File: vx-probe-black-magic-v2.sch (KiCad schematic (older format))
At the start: 14 parts, among them P1 USB MINI B, U1 stm32f070-qfp48, Y1 8 MHz

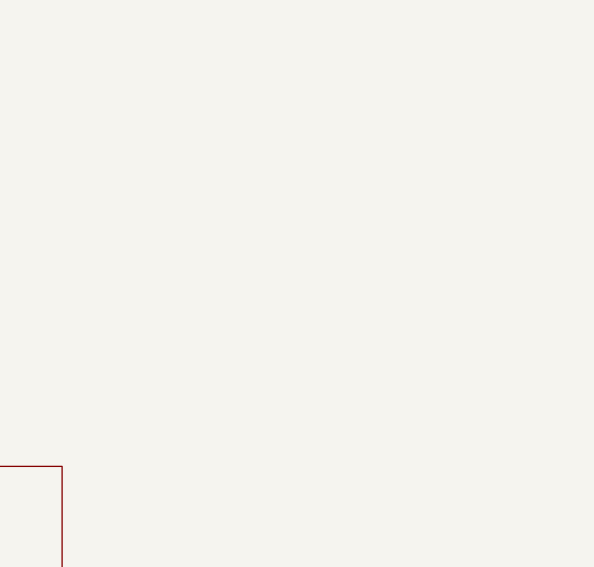
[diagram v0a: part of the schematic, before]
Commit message: added the at45db32 library part
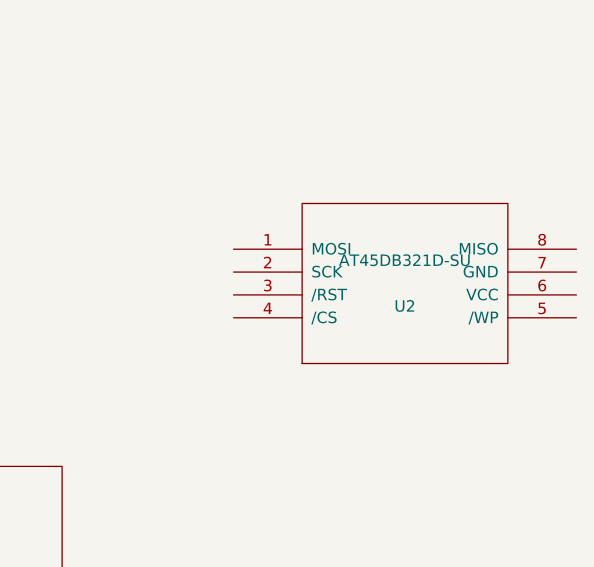
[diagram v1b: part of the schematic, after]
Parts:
- added U2: AT45DB321D-SU, MODULE, symbol AT45DB321D-SU
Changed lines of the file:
@@
 LIBS:valves
 LIBS:stm32f103-qfp48
+LIBS:AT45DB321D-SU
 LIBS:vx-probe-black-magic-v2-cache
 EELAYER 25 0
@@
 $EndComp
 $Comp
-L GND #PWR01
+L GND #PWR4
 U 1 1 57D81245
 P 2200 4200
-F 0 "#PWR01" H 2200 3950 50  0001 C CNN
+F 0 "#PWR4" H 2200 3950 50  0001 C CNN
 F 1 "GND" H 2200 4050 50  0000 C CNN
 F 2 "" H 2200 4200 50  0000 C CNN
@@
 $EndComp
 $Comp
-L +3V3 #PWR02
+L +3V3 #PWR5
 U 1 1 57D815C1
 P 2500 4500
-F 0 "#PWR02" H 2500 4350 50  0001 C CNN
+F 0 "#PWR5" H 2500 4350 50  0001 C CNN
 F 1 "+3V3" H 2500 4640 50  0000 C CNN
 F 2 "" H 2500 4500 50  0000 C CNN
@@
 $EndComp
 $Comp
-L GND #PWR03
+L GND #PWR6
 U 1 1 57D81629
 P 2500 5250
-F 0 "#PWR03" H 2500 5000 50  0001 C CNN
+F 0 "#PWR6" H 2500 5000 50  0001 C CNN
 F 1 "GND" H 2500 5100 50  0000 C CNN
 F 2 "" H 2500 5250 50  0000 C CNN
@@
 Connection ~ 1550 6900
 $Comp
-L +3V3 #PWR04
+L +3V3 #PWR1
 U 1 1 57D827E5
 P 1550 6850
-F 0 "#PWR04" H 1550 6700 50  0001 C CNN
+F 0 "#PWR1" H 1550 6700 50  0001 C CNN
 F 1 "+3V3" H 1550 6990 50  0000 C CNN
 F 2 "" H 1550 6850 50  0000 C CNN
@@
 Connection ~ 1550 7200
 $Comp
-L GND #PWR05
+L GND #PWR2
 U 1 1 57D82853
 P 1550 7250
-F 0 "#PWR05" H 1550 7000 50  0001 C CNN
+F 0 "#PWR2" H 1550 7000 50  0001 C CNN
 F 1 "GND" H 1550 7100 50  0000 C CNN
 F 2 "" H 1550 7250 50  0000 C CNN
@@
 	1950 1550 1950 1600
 $Comp
-L GND #PWR06
+L GND #PWR3
 U 1 1 57D8325D
 P 1950 1600
-F 0 "#PWR06" H 1950 1350 50  0001 C CNN
+F 0 "#PWR3" H 1950 1350 50  0001 C CNN
 F 1 "GND" H 1950 1450 50  0000 C CNN
 F 2 "" H 1950 1600 50  0000 C CNN
@@
 Wire Notes Line
 	750  2150 750  600
+$Comp
+L AT45DB321D-SU U2
+U 1 1 57D84EBF
+P 8500 1850
+F 0 "U2" H 8500 1750 50  0000 C CNN
+F 1 "AT45DB321D-SU" H 8500 1950 50  0000 C CNN
+F 2 "MODULE" H 8500 1850 50  0001 C CNN
+F 3 "DOCUMENTATION" H 8500 1850 50  0001 C CNN
+	1    8500 1850
+	1    0    0    -1
+$EndComp
 $EndSCHEMATC

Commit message: assigned the at45db32 part footprint
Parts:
- U2: footprint MODULE -> Housings_SOIC:SOIJ-8_5.3x5.3mm_Pitch1.27mm
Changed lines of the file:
@@
 $EndComp
 $Comp
-L GND #PWR4
+L GND #PWR01
 U 1 1 57D81245
 P 2200 4200
-F 0 "#PWR4" H 2200 3950 50  0001 C CNN
+F 0 "#PWR01" H 2200 3950 50  0001 C CNN
 F 1 "GND" H 2200 4050 50  0000 C CNN
 F 2 "" H 2200 4200 50  0000 C CNN
@@
 $EndComp
 $Comp
-L +3V3 #PWR5
+L +3V3 #PWR02
 U 1 1 57D815C1
 P 2500 4500
-F 0 "#PWR5" H 2500 4350 50  0001 C CNN
+F 0 "#PWR02" H 2500 4350 50  0001 C CNN
 F 1 "+3V3" H 2500 4640 50  0000 C CNN
 F 2 "" H 2500 4500 50  0000 C CNN
@@
 $EndComp
 $Comp
-L GND #PWR6
+L GND #PWR03
 U 1 1 57D81629
 P 2500 5250
-F 0 "#PWR6" H 2500 5000 50  0001 C CNN
+F 0 "#PWR03" H 2500 5000 50  0001 C CNN
 F 1 "GND" H 2500 5100 50  0000 C CNN
 F 2 "" H 2500 5250 50  0000 C CNN
@@
 Connection ~ 1550 6900
 $Comp
-L +3V3 #PWR1
+L +3V3 #PWR04
 U 1 1 57D827E5
 P 1550 6850
-F 0 "#PWR1" H 1550 6700 50  0001 C CNN
+F 0 "#PWR04" H 1550 6700 50  0001 C CNN
 F 1 "+3V3" H 1550 6990 50  0000 C CNN
 F 2 "" H 1550 6850 50  0000 C CNN
@@
 Connection ~ 1550 7200
 $Comp
-L GND #PWR2
+L GND #PWR05
 U 1 1 57D82853
 P 1550 7250
-F 0 "#PWR2" H 1550 7000 50  0001 C CNN
+F 0 "#PWR05" H 1550 7000 50  0001 C CNN
 F 1 "GND" H 1550 7100 50  0000 C CNN
 F 2 "" H 1550 7250 50  0000 C CNN
@@
 	1950 1550 1950 1600
 $Comp
-L GND #PWR3
+L GND #PWR06
 U 1 1 57D8325D
 P 1950 1600
-F 0 "#PWR3" H 1950 1350 50  0001 C CNN
+F 0 "#PWR06" H 1950 1350 50  0001 C CNN
 F 1 "GND" H 1950 1450 50  0000 C CNN
 F 2 "" H 1950 1600 50  0000 C CNN
@@
 F 0 "U2" H 8500 1750 50  0000 C CNN
 F 1 "AT45DB321D-SU" H 8500 1950 50  0000 C CNN
-F 2 "MODULE" H 8500 1850 50  0001 C CNN
+F 2 "Housings_SOIC:SOIJ-8_5.3x5.3mm_Pitch1.27mm" H 8500 1850 50  0001 C CNN
 F 3 "DOCUMENTATION" H 8500 1850 50  0001 C CNN
 	1    8500 1850

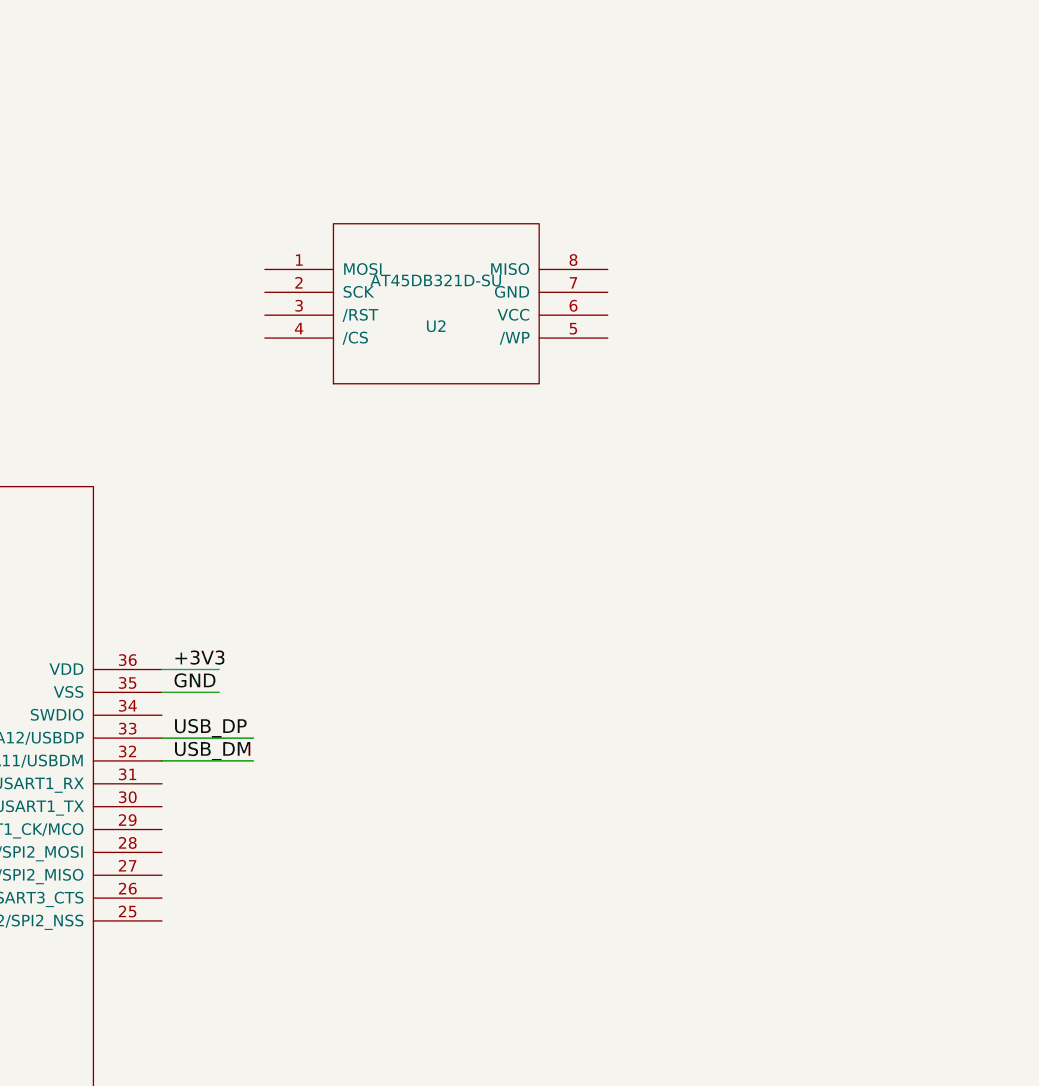
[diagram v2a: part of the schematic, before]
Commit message: wired up the external spi memory
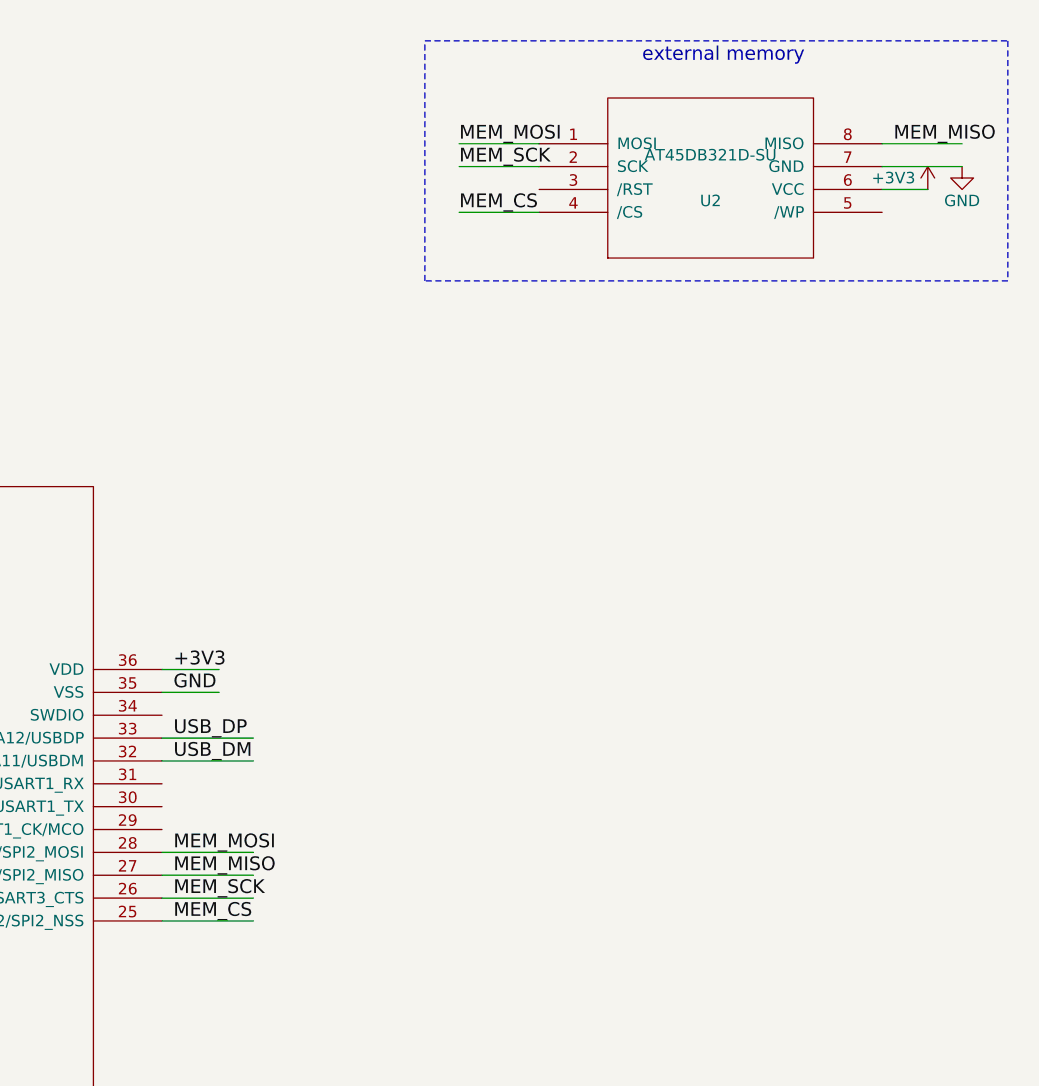
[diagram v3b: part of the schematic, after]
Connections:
- net labels added: MEM_CS, MEM_MISO, MEM_MOSI, MEM_SCK
- wire segments 46 -> 56
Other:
- note added: "external memory"
- moved on the sheet: U2
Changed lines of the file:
@@
 L AT45DB321D-SU U2
 U 1 1 57D84EBF
-P 8500 1850
-F 0 "U2" H 8500 1750 50  0000 C CNN
-F 1 "AT45DB321D-SU" H 8500 1950 50  0000 C CNN
-F 2 "Housings_SOIC:SOIJ-8_5.3x5.3mm_Pitch1.27mm" H 8500 1850 50  0001 C CNN
-F 3 "DOCUMENTATION" H 8500 1850 50  0001 C CNN
-	1    8500 1850
+P 9700 1300
+F 0 "U2" H 9700 1200 50  0000 C CNN
+F 1 "AT45DB321D-SU" H 9700 1400 50  0000 C CNN
+F 2 "Housings_SOIC:SOIJ-8_5.3x5.3mm_Pitch1.27mm" H 9700 1300 50  0001 C CNN
+F 3 "DOCUMENTATION" H 9700 1300 50  0001 C CNN
+	1    9700 1300
 	1    0    0    -1
 $EndComp
+Wire Wire Line
+	10800 1150 10450 1150
+Wire Wire Line
+	10800 1250 10450 1250
+Wire Wire Line
+	8950 1150 8600 1150
+Wire Wire Line
+	8950 1250 8600 1250
+Wire Wire Line
+	8950 1450 8600 1450
+Text Label 8600 1450 0    60   ~ 0
+MEM_CS
+Text Label 8600 1150 0    60   ~ 0
+MEM_MOSI
+Text Label 8600 1250 0    60   ~ 0
+MEM_SCK
+Text Label 10500 1150 0    60   ~ 0
+MEM_MISO
+Wire Wire Line
+	10450 1350 10650 1350
+$Comp
+L +3V3 #PWR?
+U 1 1 57D8566A
+P 10650 1350
+F 0 "#PWR?" H 10650 1200 50  0001 C CNN
+F 1 "+3V3" H 10500 1400 50  0000 C CNN
+F 2 "" H 10650 1350 50  0000 C CNN
+F 3 "" H 10650 1350 50  0000 C CNN
+	1    10650 1350
+	1    0    0    -1
+$EndComp
+$Comp
+L GND #PWR?
+U 1 1 57D856D3
+P 10800 1250
+F 0 "#PWR?" H 10800 1000 50  0001 C CNN
+F 1 "GND" H 10800 1100 50  0000 C CNN
+F 2 "" H 10800 1250 50  0000 C CNN
+F 3 "" H 10800 1250 50  0000 C CNN
+	1    10800 1250
+	1    0    0    -1
+$EndComp
+Wire Wire Line
+	7300 4250 7700 4250
+Wire Wire Line
+	7300 4350 7700 4350
+Wire Wire Line
+	7300 4450 7700 4450
+Wire Wire Line
+	7300 4550 7700 4550
+Text Label 7350 4350 0    60   ~ 0
+MEM_MISO
+Text Label 7350 4250 0    60   ~ 0
+MEM_MOSI
+Text Label 7350 4450 0    60   ~ 0
+MEM_SCK
+Text Label 7350 4550 0    60   ~ 0
+MEM_CS
+Text Notes 9400 800  0    60   ~ 0
+external memory
+Wire Notes Line
+	8450 700  11000 700
+Wire Notes Line
+	11000 700  11000 1750
+Wire Notes Line
+	11000 1750 8450 1750
+Wire Notes Line
+	8450 1750 8450 700
 $EndSCHEMATC

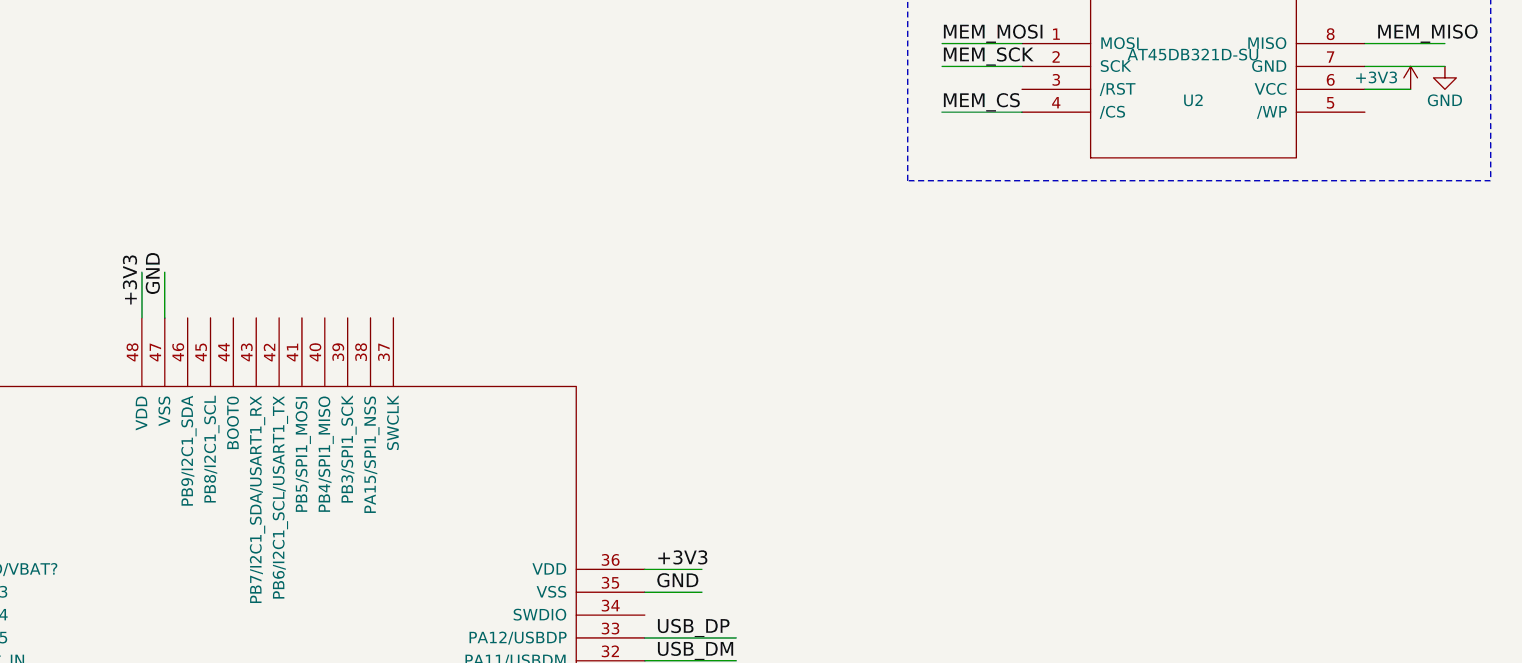
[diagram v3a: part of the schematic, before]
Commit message: wired up the olimex UEXT port
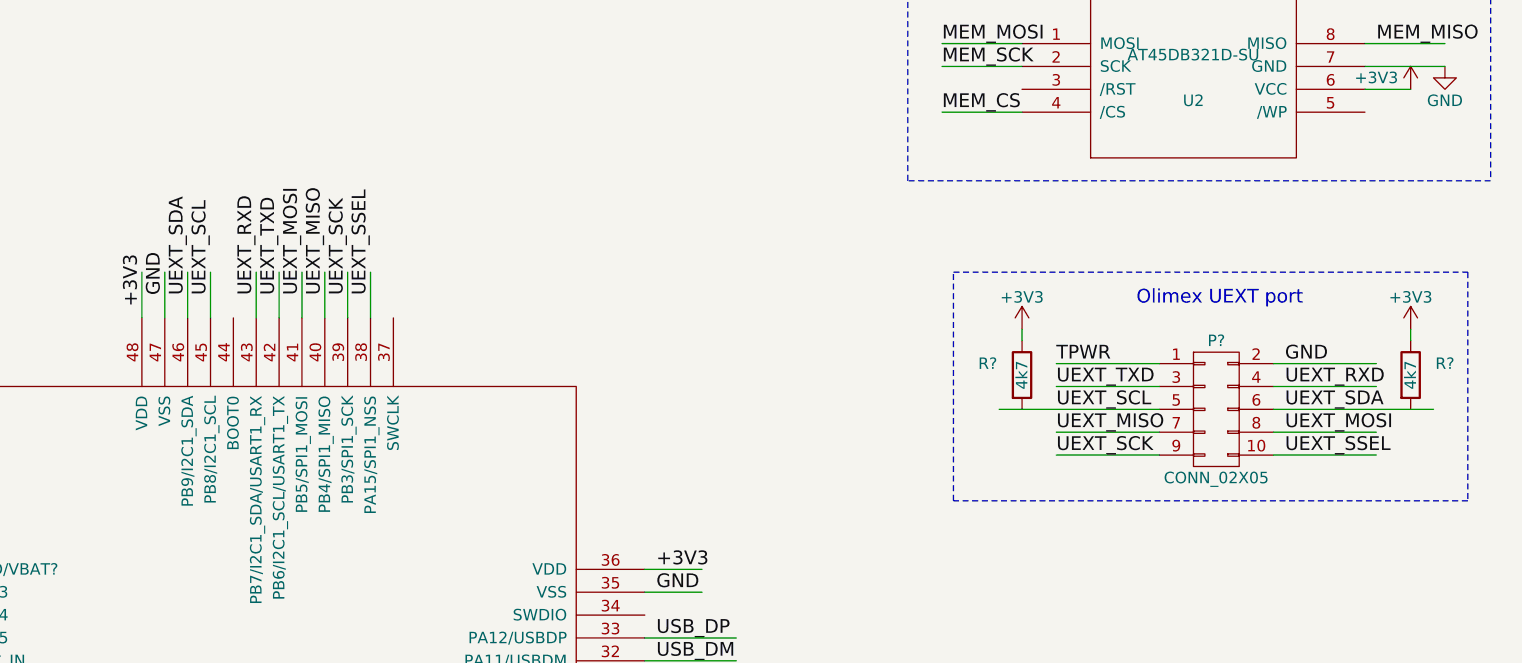
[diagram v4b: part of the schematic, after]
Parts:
- added P?: CONN_02X05, symbol CONN_02X05
- added R? (x2): 4k7, symbol R
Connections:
- net labels added: TPWR, UEXT_MISO, UEXT_MOSI, UEXT_RXD, UEXT_SCK, UEXT_SCL, UEXT_SDA, UEXT_SSEL, UEXT_TXD
- wire segments 56 -> 76
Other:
- note added: "Olimex UEXT port"
